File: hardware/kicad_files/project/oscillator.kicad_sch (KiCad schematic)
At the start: 3 parts, among them X1 TXM12M0004252DBCEO00T

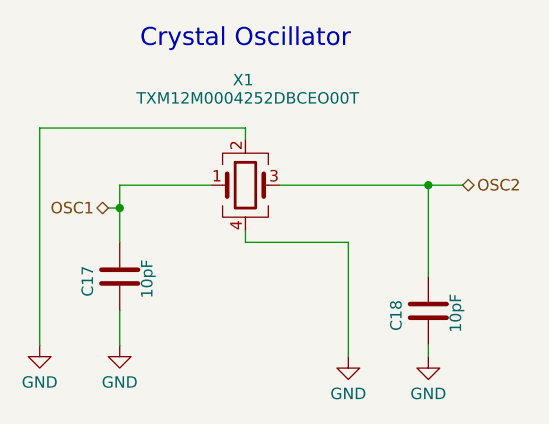
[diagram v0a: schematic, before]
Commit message: feat: update to 0.2
feat: add pin sockets compatible to the Pmod interface

feat: add a power switch and an overcurrent protection circuit, including a fault status LED and a solder bridge

fix: remove the clock jumpers and directly connect the second output clock to the user clock input

misc: remove the jumpers from io 36 and 37 to the bitbang inputs, add bitbang pins to the UART connector

cosmetic: make the PCB edges round
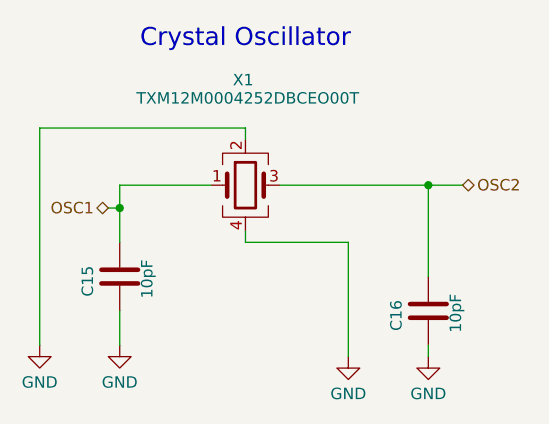
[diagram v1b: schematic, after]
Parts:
- renumbered C17 to C15, C18 to C16
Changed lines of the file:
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@@
 	(title_block
 		(date "2024-05-30")
-		(rev "0.1.1")
+		(rev "0.2.0")
 	)
 	(junction
@@
 		(dnp no)
 		(fields_autoplaced yes)
-		(property "Reference" "#PWR055"
+		(property "Reference" "#PWR53"
 			(at 123.19 113.03 0)
 			(effects
@@
 			(project "FABulous_board"
 				(path "/5664f05e-a3ef-4177-8026-c4580fa32c71/b4d9b251-031a-4875-8b01-0478a187070c/4c7542bb-a835-445d-b466-6e95b674eb44"
-					(reference "#PWR055")
+					(reference "#PWR53")
 					(unit 1)
 				)
@@
 		(dnp no)
 		(fields_autoplaced yes)
-		(property "Reference" "#PWR054"
+		(property "Reference" "#PWR52"
 			(at 114.3 113.03 0)
 			(effects
@@
 			(project "FABulous_board"
 				(path "/5664f05e-a3ef-4177-8026-c4580fa32c71/b4d9b251-031a-4875-8b01-0478a187070c/4c7542bb-a835-445d-b466-6e95b674eb44"
-					(reference "#PWR054")
+					(reference "#PWR52")
 					(unit 1)
 				)
@@
 		(dnp no)
 		(fields_autoplaced yes)
-		(property "Reference" "#PWR056"
+		(property "Reference" "#PWR54"
 			(at 148.59 114.3 0)
 			(effects
@@
 			(project "FABulous_board"
 				(path "/5664f05e-a3ef-4177-8026-c4580fa32c71/b4d9b251-031a-4875-8b01-0478a187070c/4c7542bb-a835-445d-b466-6e95b674eb44"
-					(reference "#PWR056")
+					(reference "#PWR54")
 					(unit 1)
 				)
@@
 		(dnp no)
 		(fields_autoplaced yes)
-		(property "Reference" "#PWR057"
+		(property "Reference" "#PWR55"
 			(at 157.48 114.3 0)
 			(effects
@@
 			(project "FABulous_board"
 				(path "/5664f05e-a3ef-4177-8026-c4580fa32c71/b4d9b251-031a-4875-8b01-0478a187070c/4c7542bb-a835-445d-b466-6e95b674eb44"
-					(reference "#PWR057")
+					(reference "#PWR55")
 					(unit 1)
 				)
@@
 		(on_board yes)
 		(dnp no)
-		(property "Reference" "C18"
+		(property "Reference" "C16"
 			(at 153.924 103.378 90)
 			(effects
@@
 			(project "FABulous_board"
 				(path "/5664f05e-a3ef-4177-8026-c4580fa32c71/b4d9b251-031a-4875-8b01-0478a187070c/4c7542bb-a835-445d-b466-6e95b674eb44"
-					(reference "C18")
+					(reference "C16")
 					(unit 1)
 				)
@@
 		(on_board yes)
 		(dnp no)
-		(property "Reference" "C17"
+		(property "Reference" "C15"
 			(at 119.634 99.568 90)
 			(effects
@@
 			(project "FABulous_board"
 				(path "/5664f05e-a3ef-4177-8026-c4580fa32c71/b4d9b251-031a-4875-8b01-0478a187070c/4c7542bb-a835-445d-b466-6e95b674eb44"
-					(reference "C17")
+					(reference "C15")
 					(unit 1)
 				)
